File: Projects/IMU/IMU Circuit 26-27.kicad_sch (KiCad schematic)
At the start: 13 parts, among them U1 TJA1050DRG, U2 MCP2515-I, U3 TM171, X1 ${ALTIUM_VALUE}

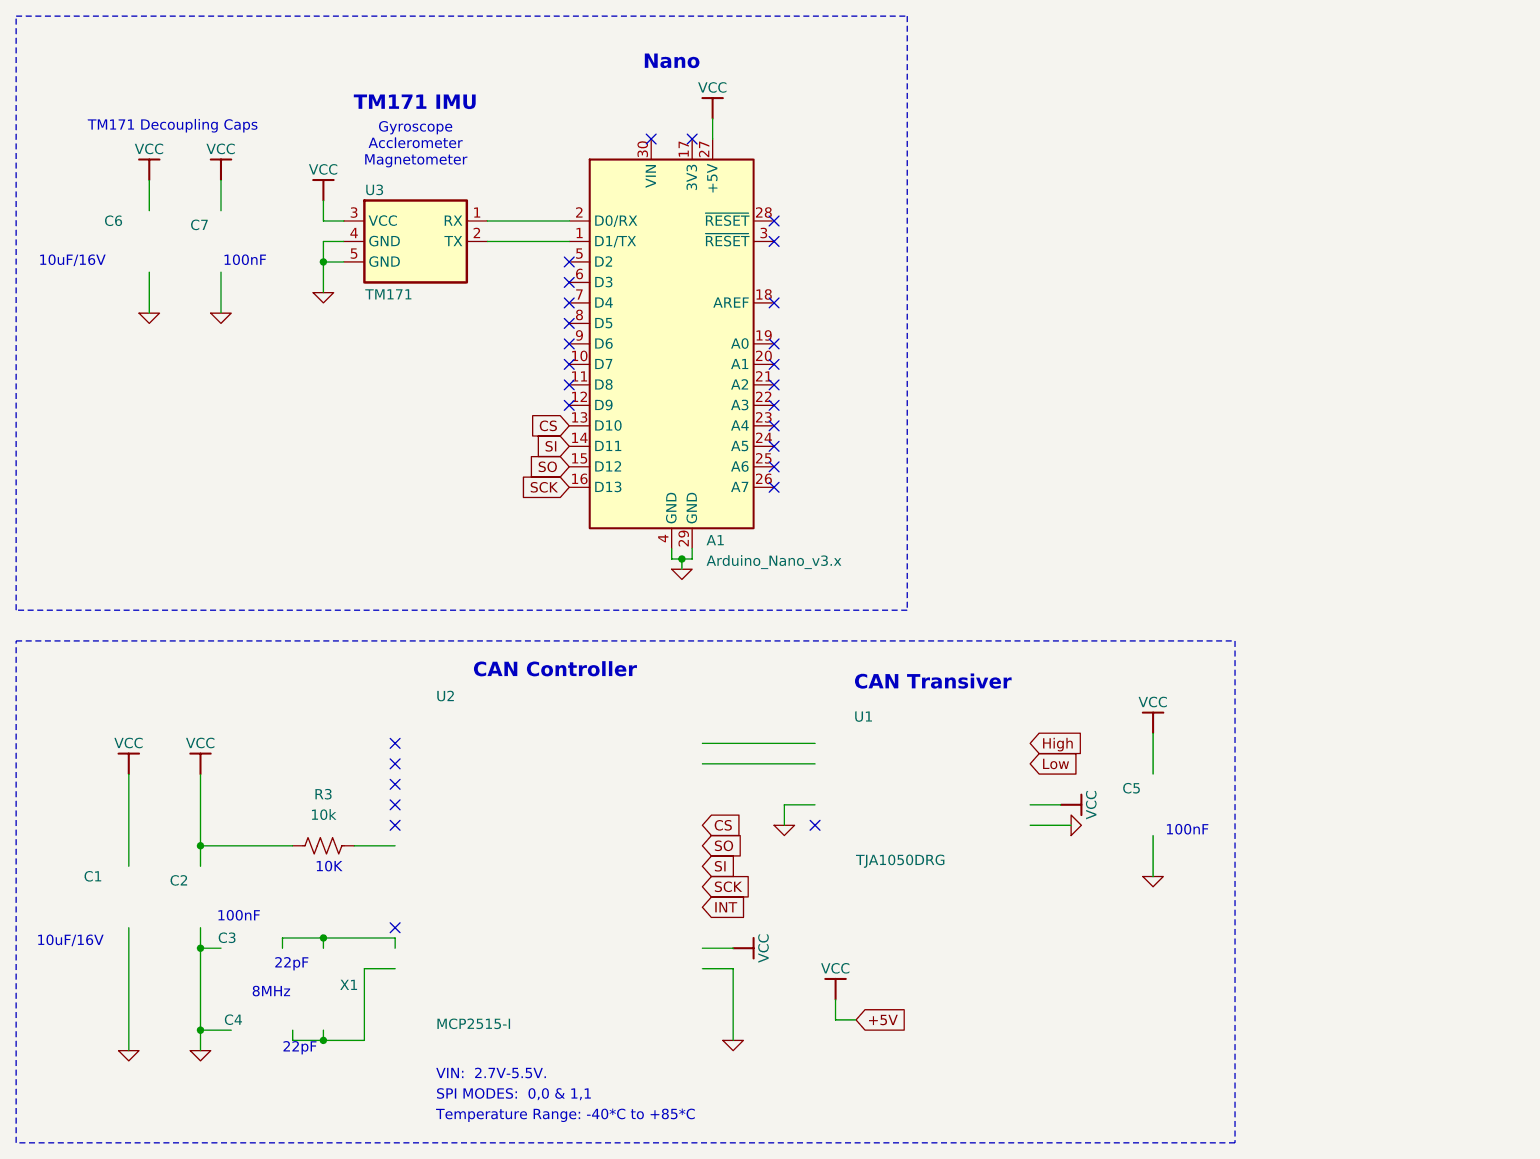
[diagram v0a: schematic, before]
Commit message: the pcb update
(mostly) done routing, fill areas, and silkscreens
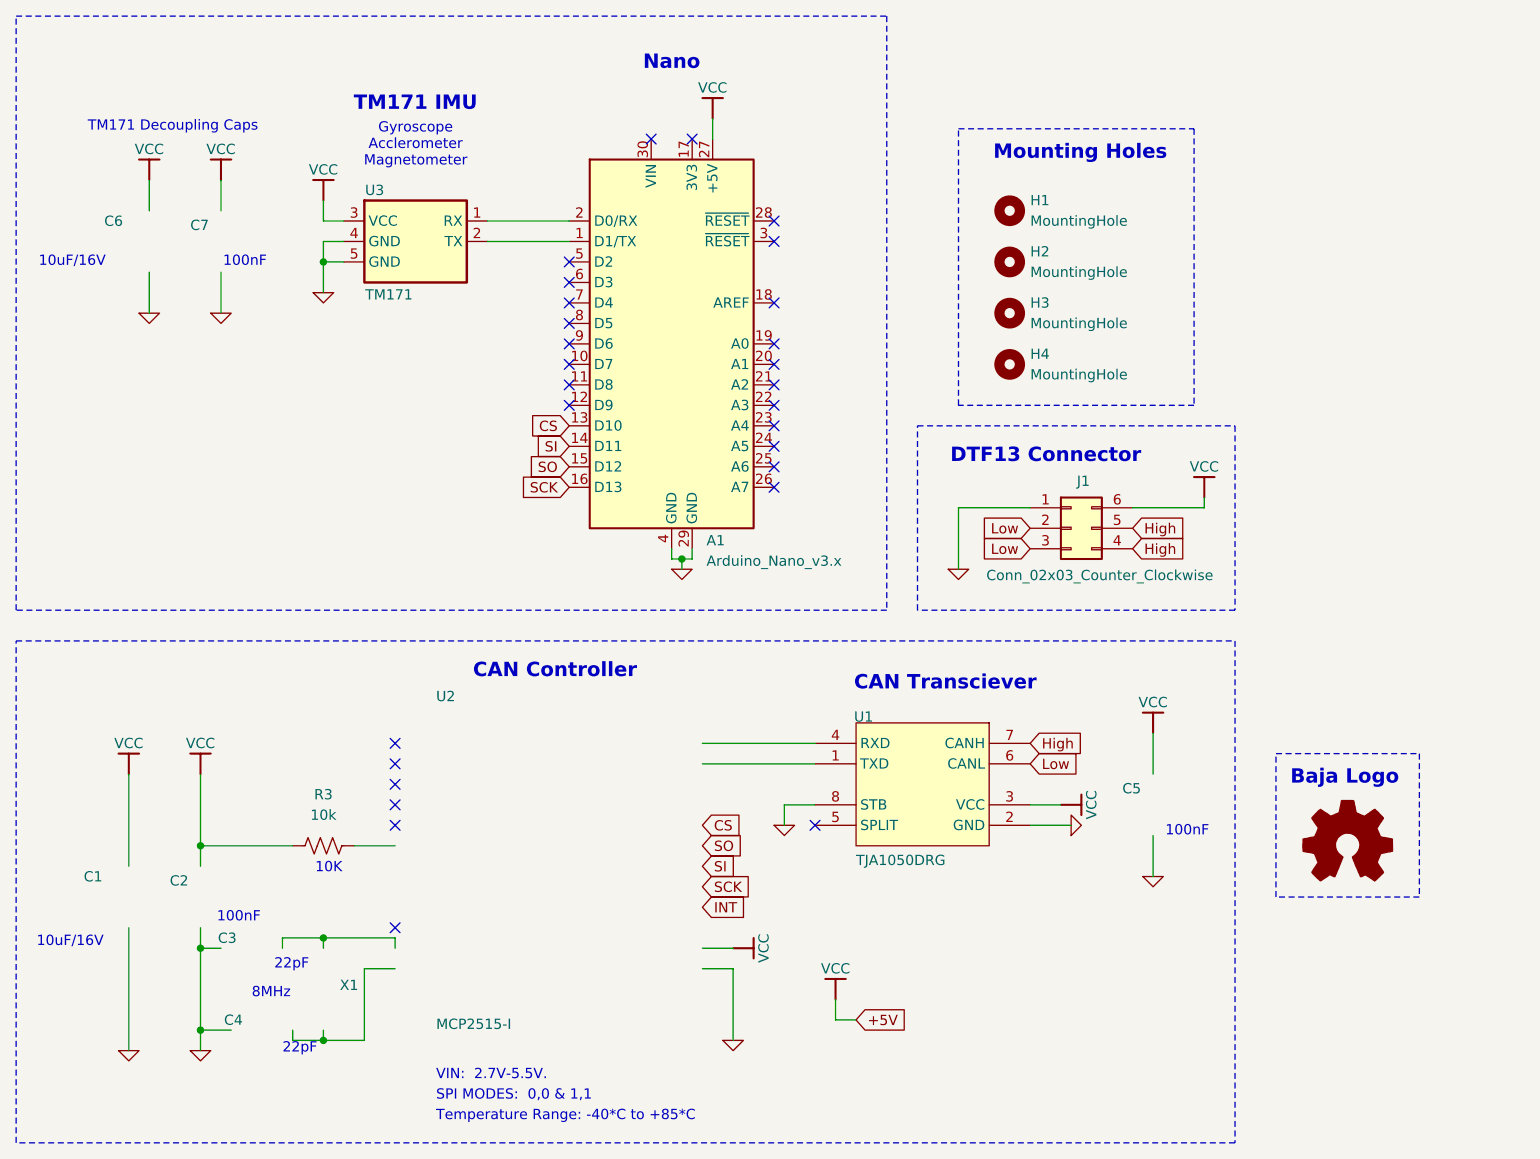
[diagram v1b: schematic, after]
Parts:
- added H1, H2, H3, H4: MountingHole, MountingHole:MountingHole_3.2mm_M3, symbol Mechanical:MountingHole
- added J1: Conn_02x03_Counter_Clockwise, DTF13:TE_DTF13-6P, symbol Connector_Generic:Conn_02x03_Counter_Clockwise
- added Logo1: Logo_Open_Hardware_Small, Baja Logo for PCB:Baja Logo, symbol Graphic:Logo_Open_Hardware_Small
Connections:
- net 0: now also U1.2 (GND), U1.8 (STB), J1.1 (Pin_1)
- net High: now also U1.7 (CANH), J1.4 (Pin_4), J1.5 (Pin_5)
- net Low: now also U1.6 (CANL), J1.2 (Pin_2), J1.3 (Pin_3)
- net VCC: now also U1.3 (VCC), J1.6 (Pin_6)
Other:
- note added: "Baja Logo"
- note added: "CAN Transciever"
- note added: "DTF13 Connector"
- note added: "Mounting Holes"
- note removed: "CAN Transiver"
- company: UA BAJA- Graham VanDerBeek -> UA BAJA- Johnathan Guzman
- title: CAN Circuit 26-27 -> IMU Circuit 26-27

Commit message: connected int for can controller
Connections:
- net INT: now also A1.5 (D2)
- no-connect marks 28 -> 27
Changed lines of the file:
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@@
-	)
-	(no_connect
-		(at 90.17 83.82)
 	)
 	(no_connect
@@
 		(property "Intersheetrefs" "${INTERSHEET_REFS}"
 			(at 84.6448 109.22 0)
+			(hide yes)
+			(show_name no)
+			(do_not_autoplace no)
+			(effects
+				(font
+					(size 1.27 1.27)
+				)
+				(justify right)
+			)
+		)
+	)
+	(global_label "INT"
+		(shape input)
+		(at 90.17 83.82 180)
+		(fields_autoplaced yes)
+		(effects
+			(font
+				(size 1.27 1.27)
+			)
+			(justify right)
+		)
+		(property "Intersheetrefs" "${INTERSHEET_REFS}"
+			(at 84.2819 83.82 0)
 			(hide yes)
 			(show_name no)
@@
 		(unit 1)
 		(body_style 1)
-		(exclude_from_sim no)
+		(exclude_from_sim yes)
 		(in_bom no)
 		(on_board no)
@@
 			(at 186.69 156.21 0)
 			(hide yes)
-			(show_name no)
-			(do_not_autoplace no)
-			(effects
-				(font
-					(size 1.27 1.27)
-				)
-			)
-		)
-		(property "Sim.Enable" "0"
-			(at 186.69 156.21 0)
-			(hide yes)

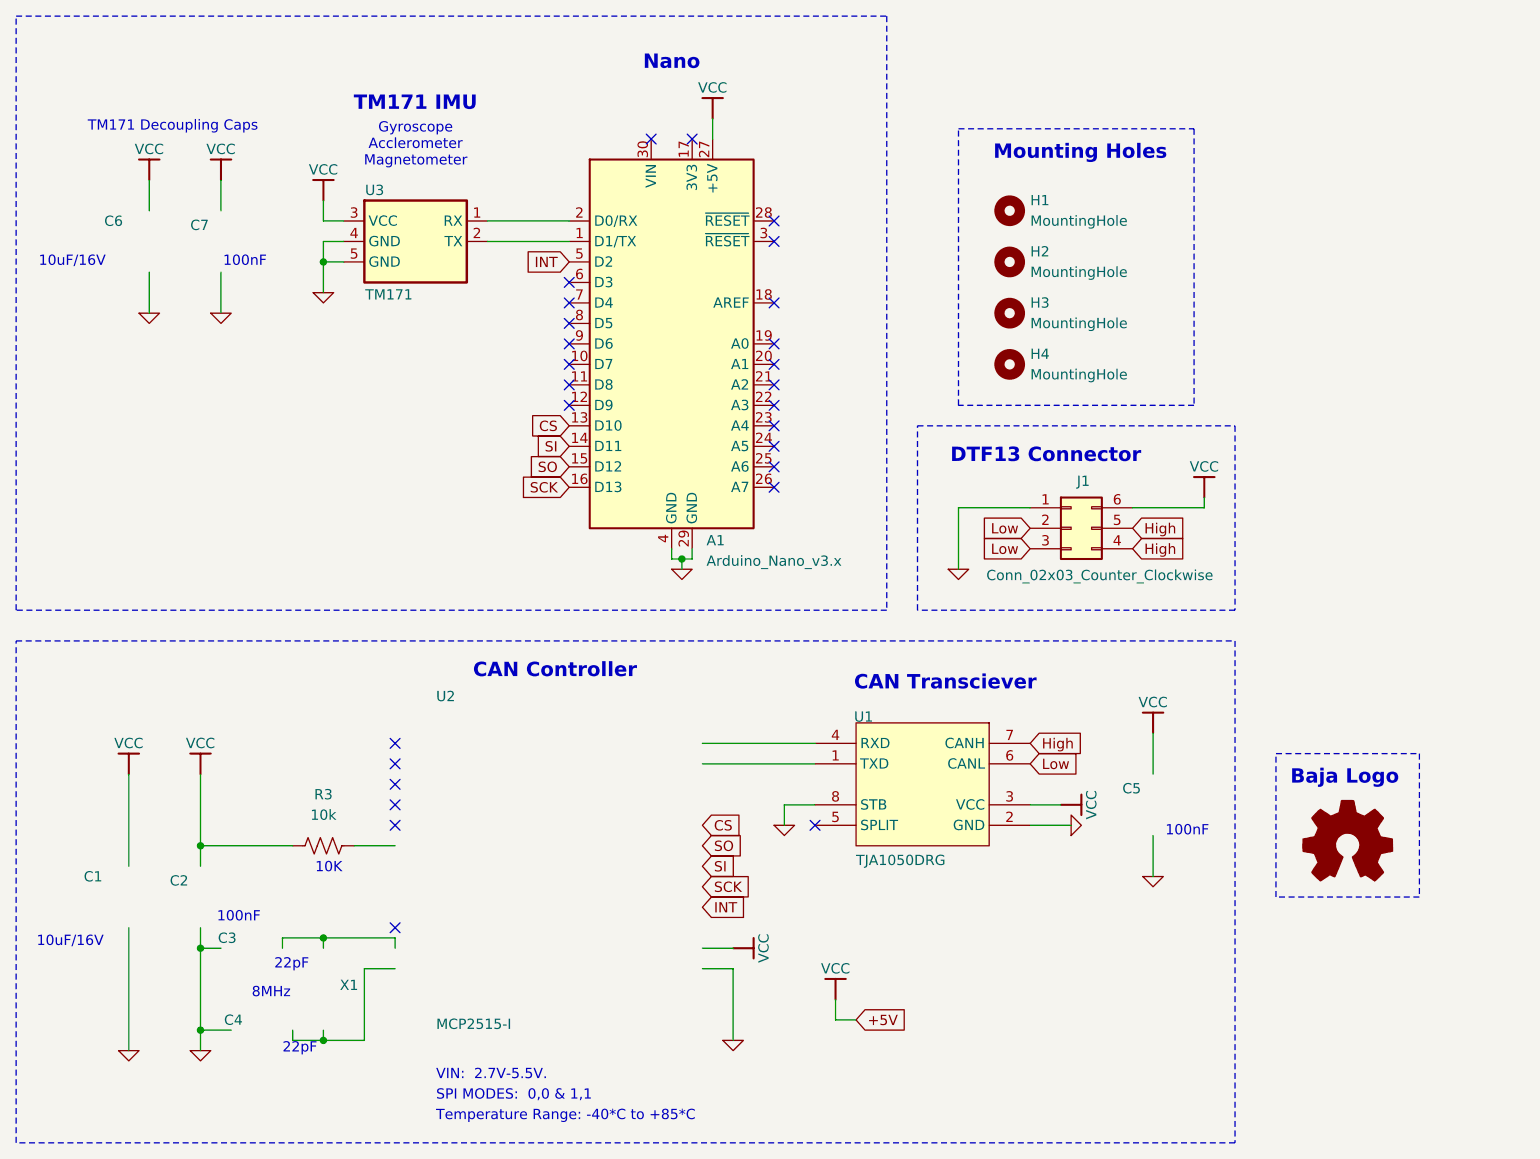
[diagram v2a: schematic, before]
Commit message: moved some mounting holes
one hole no longer under DTF conn
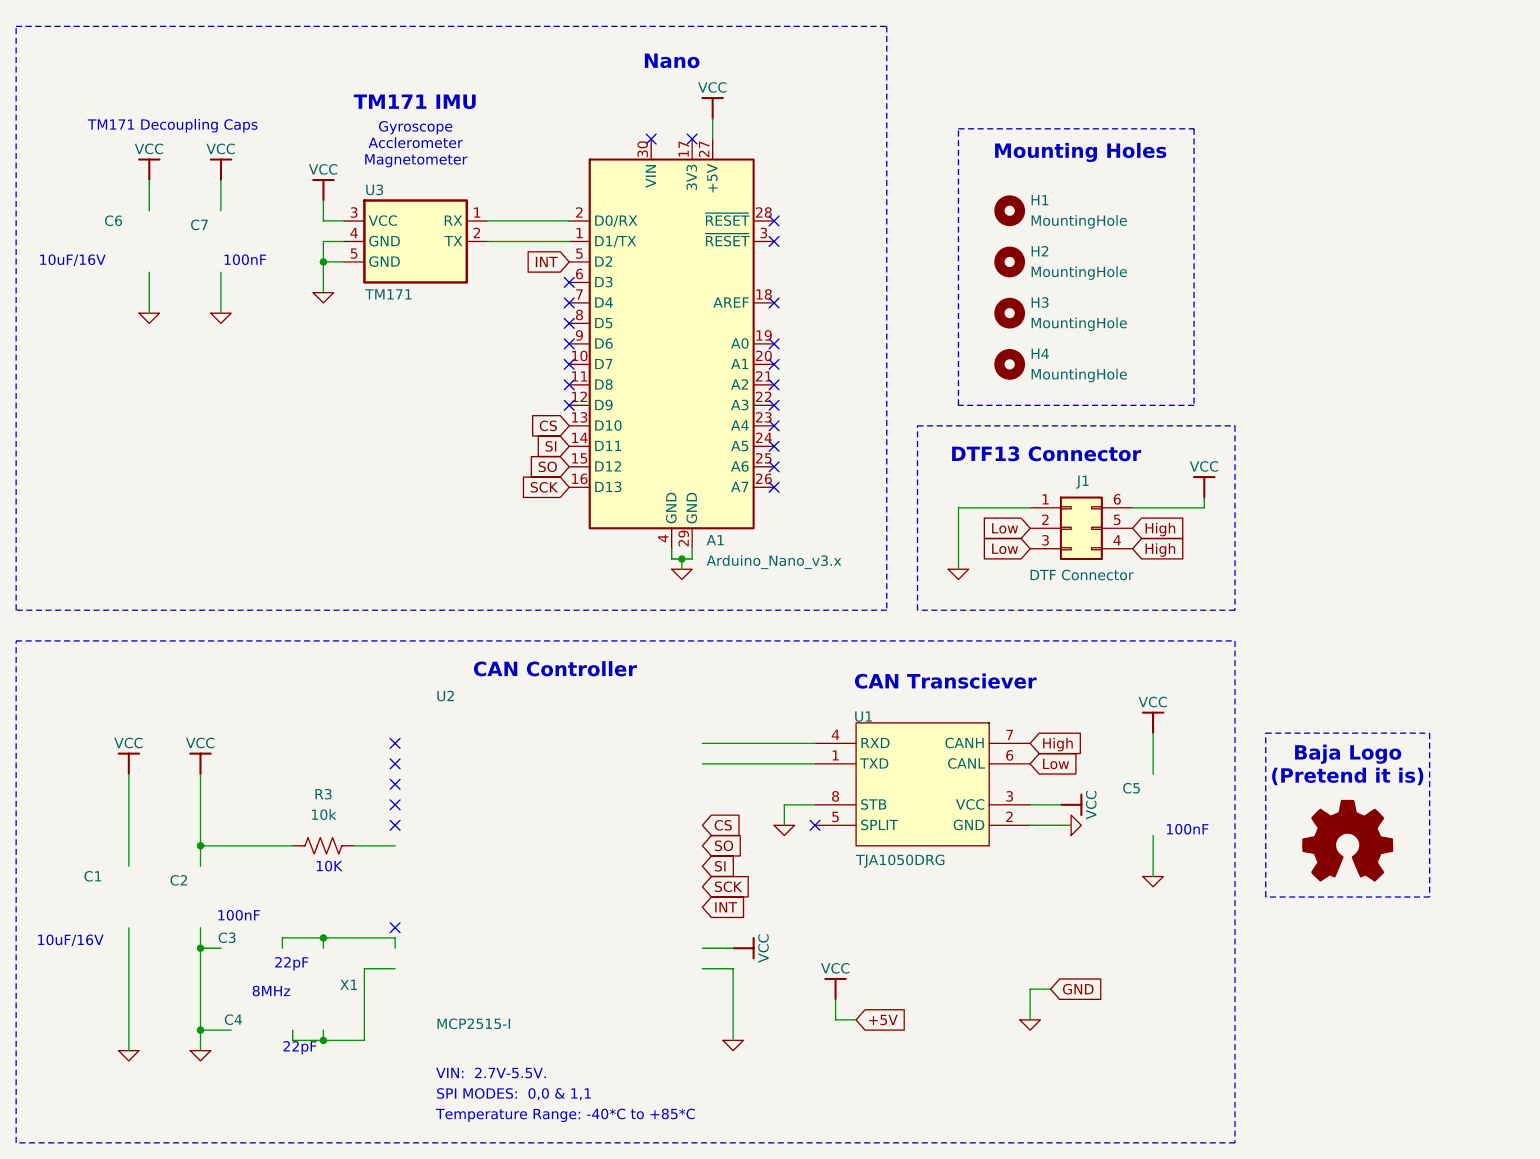
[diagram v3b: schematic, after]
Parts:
- J1: value Conn_02x03_Counter_Clockwise -> DTF Connector
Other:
- note added: "Baja Logo (Pretend it is)"
- note removed: "Baja Logo"
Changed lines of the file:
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@@
 	)
 	(rectangle
-		(start 21.59 53.34)
+		(start 21.59 54.61)
 		(end 129.54 127)
 		(stroke
@@
 	)
 	(rectangle
-		(start 177.8 144.78)
-		(end 195.58 162.56)
+		(start 176.53 142.24)
+		(end 196.85 162.56)
 		(stroke
 			(width 0)
@@
 		)
 	)
-	(text "Baja Logo"
+	(text "Baja Logo\n(Pretend it is)"
 		(exclude_from_sim no)
-		(at 179.578 148.844 0)
+		(at 186.69 148.844 0)
 		(effects
 			(font
@@
 				(bold yes)
 			)
-			(justify left bottom)
+			(justify bottom)
 		)
 	)
@@
 	(wire
 		(pts
+			(xy 149.86 173.99) (xy 147.32 173.99)
+		)
+		(stroke
+			(width 0)
+			(type default)
+		)
+	)
+	(wire
+		(pts
 			(xy 59.69 83.82) (xy 62.23 83.82)
 		)
@@
 	(wire
 		(pts
+			(xy 147.32 173.99) (xy 147.32 177.8)
+		)
+		(stroke
+			(width 0)
+			(type default)
+		)
+	)
+	(wire
+		(pts
 			(xy 110.49 171.45) (xy 106.68 171.45)
 		)
@@
 		)
 	)
+	(global_label "GND"
+		(shape input)
+		(at 149.86 173.99 0)
+		(fields_autoplaced yes)
+		(effects
+			(font
+				(size 1.27 1.27)
+			)
+			(justify left)
+		)
+		(property "Intersheetrefs" "${INTERSHEET_REFS}"
+			(at 156.7157 173.99 0)
+			(hide yes)
+			(show_name no)
+			(do_not_autoplace no)
+			(effects
+				(font
+					(size 1.27 1.27)
+				)
+				(justify left)
+			)
+		)
+	)
 	(symbol
 		(lib_id "Mechanical:MountingHole")
@@
 			)
 		)
-		(property "Value" "Conn_02x03_Counter_Clockwise"
-			(at 155.956 122.682 0)
+		(property "Value" "DTF Connector"
+			(at 153.67 122.682 0)
 			(show_name no)
 			(do_not_autoplace no)
@@
 					(unit 1)
 				)
+			)
+		)
+	)
+	(symbol
+		(lib_id "Simulation_SPICE:0")
+		(at 147.32 177.8 0)
+		(unit 1)
+		(body_style 1)
+		(exclude_from_sim no)
+		(in_bom yes)
+		(on_board yes)
+		(in_pos_files yes)
+		(dnp no)
+		(fields_autoplaced yes)
+		(property "Reference" "#GND024"
+			(at 147.32 182.88 0)
+			(hide yes)
+			(show_name no)
+			(do_not_autoplace no)
+			(effects
+				(font
+					(size 1.27 1.27)
+				)
+			)
+		)
+		(property "Value" "0"
+			(at 147.32 175.26 0)
+			(hide yes)
+			(show_name no)
+			(do_not_autoplace no)
+			(effects
+				(font
+					(size 1.27 1.27)
+				)
+			)
+		)
+		(property "Footprint" ""
+			(at 147.32 177.8 0)
+			(hide yes)
+			(show_name no)
+			(do_not_autoplace no)
+			(effects
+				(font
+					(size 1.27 1.27)
+				)
+			)
+		)
+		(property "Datasheet" "https://ngspice.sourceforge.io/docs/ngspice-html-manual/manual.xhtml#subsec_Circuit_elements__device"
+			(at 147.32 187.96 0)
+			(hide yes)
+			(show_name no)
+			(do_not_autoplace no)
+			(effects
+				(font
+					(size 1.27 1.27)
+				)
+			)
+		)
+		(property "Description" "0V reference potential for simulation"
+			(at 147.32 185.42 0)
+			(hide yes)
+			(show_name no)
+			(do_not_autoplace no)
+			(effects
+				(font
+					(size 1.27 1.27)
+				)
+			)
+		)
+		(pin "1"
+		)
+		(instances
+			(project "IMU Circuit 26-27"
+				(path "/d185ddb1-e4c7-4aec-9e87-37dceb424272"
+					(reference "#GND024")
+					(unit 1)
+				)
